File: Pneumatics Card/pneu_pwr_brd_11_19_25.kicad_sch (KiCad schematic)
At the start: 62 parts, among them J1 2X1, J10 Conn_01x02, J11 Conn_01x02, J12 2X1, J2 2X1, J3 2X1, J4 2X1, J5 2X1, J6 2X1, J7 Conn_01x03_Pin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

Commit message: Testing_Anthony
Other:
- note added: "NEED BJTS KEEP CAPs THE SAME for NOW HOLES VIAS VIAS VIAS"
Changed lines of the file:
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@@
 	(generator_version "9.0")
 	(paper "A2")
+	(text "NEED BJTS\nKEEP CAPs THE SAME for NOW\nHOLES\nVIAS VIAS VIAS"
+		(exclude_from_sim no)
+		(at 169.926 298.704 0)
+		(effects
+			(font
+				(size 1.27 1.27)
+			)
+		)
+	)
 	(text "HSE\n"
 		(exclude_from_sim no)

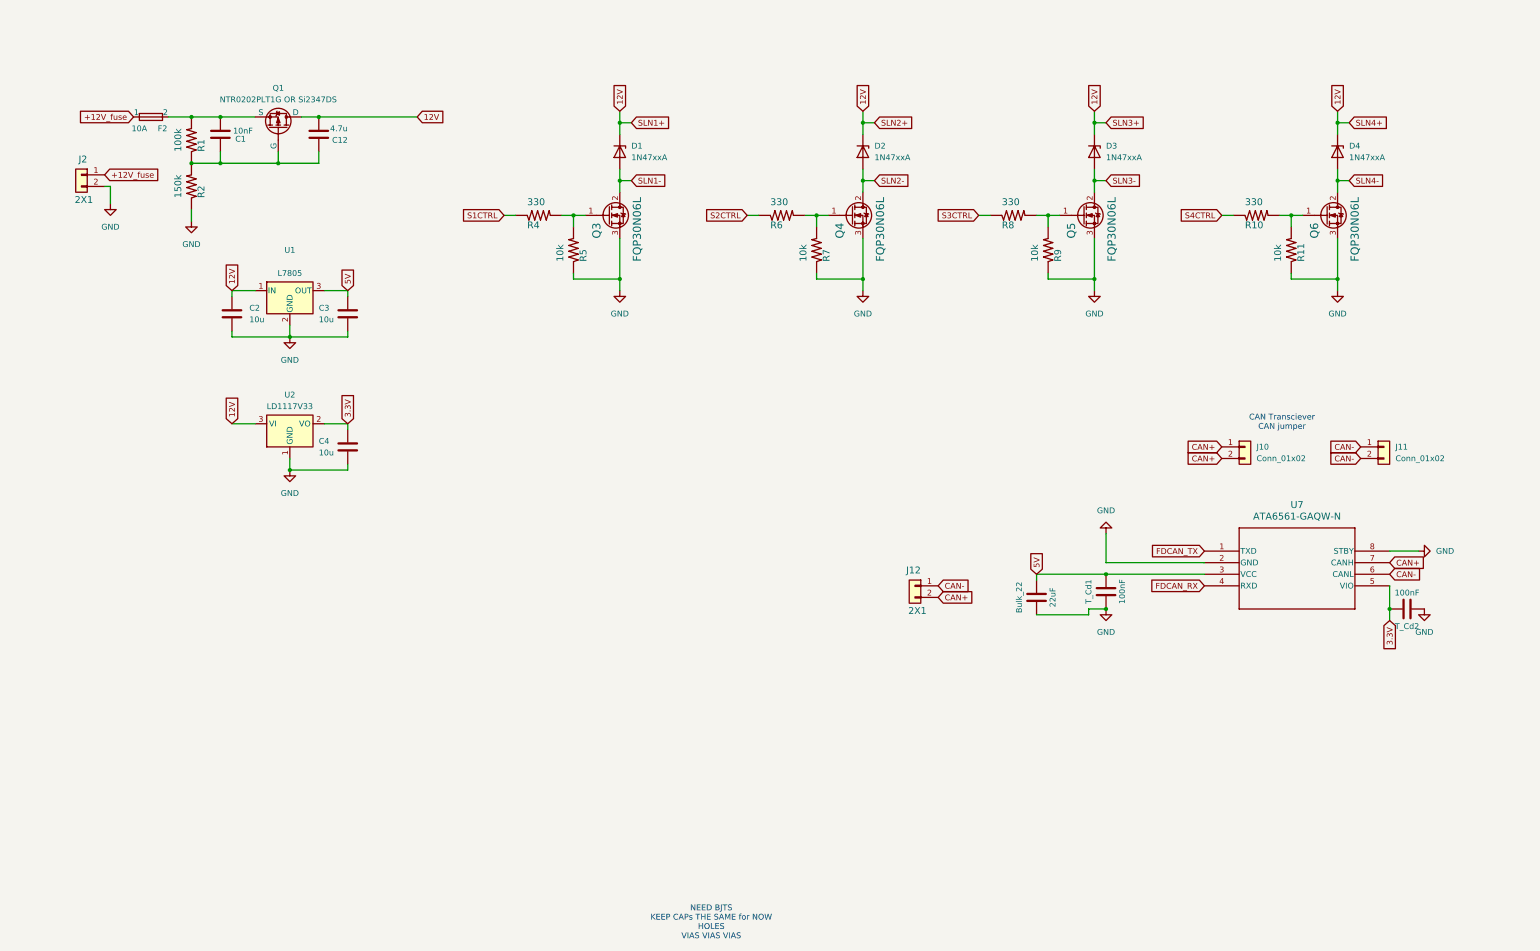
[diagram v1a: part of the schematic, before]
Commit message: Added the Mosfet drivers
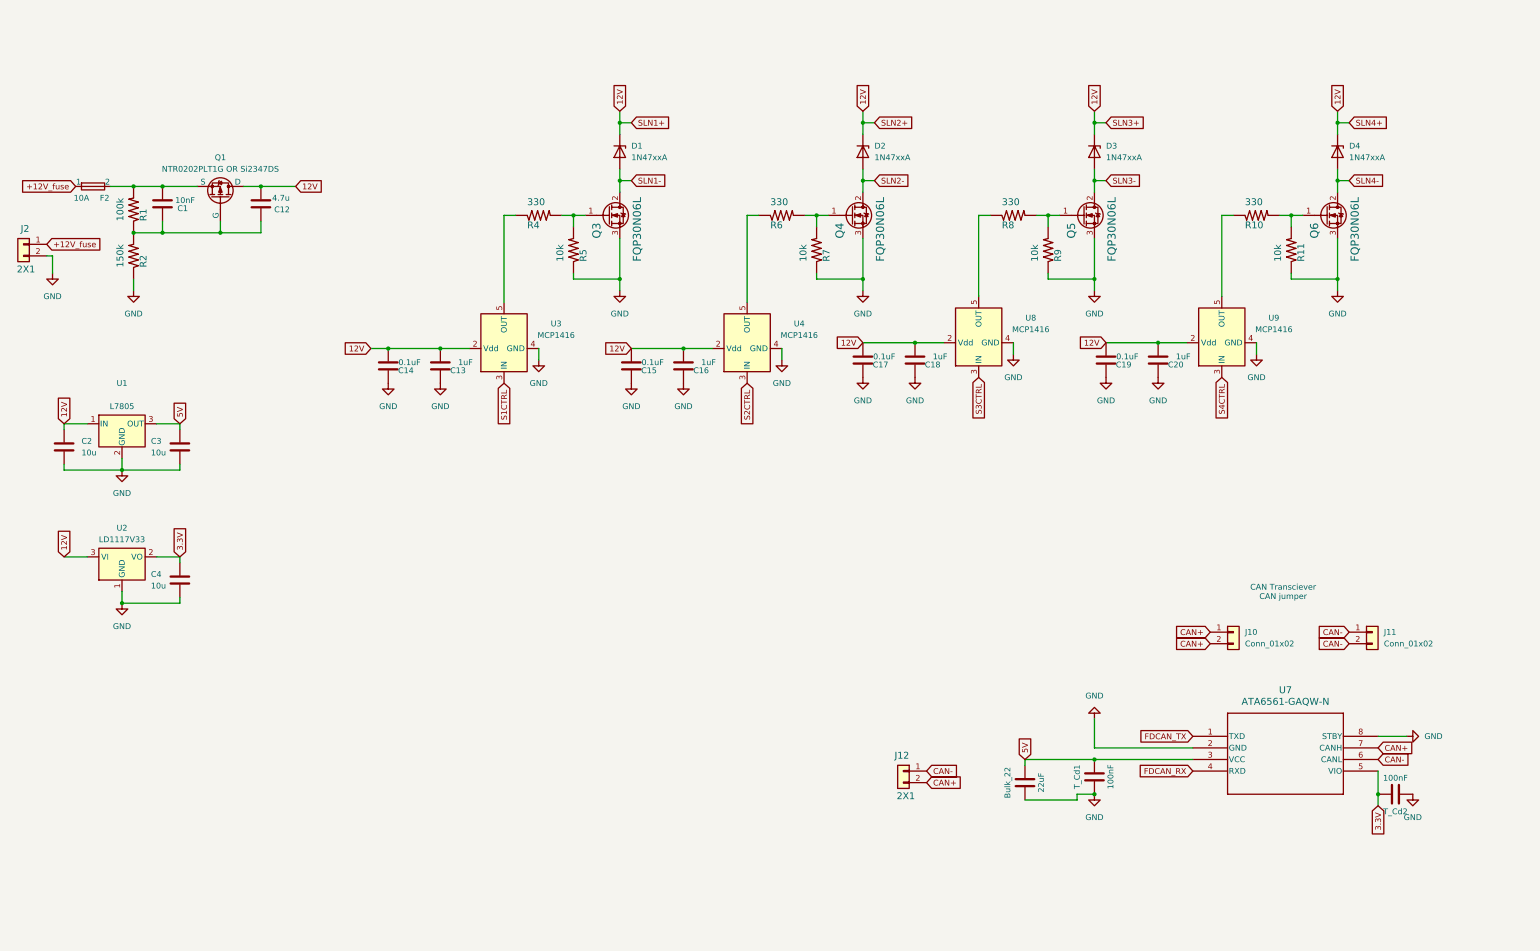
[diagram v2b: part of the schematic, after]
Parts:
- added C13, C16, C18, C20: 1uF, Capacitor_SMD:C_0402_1005Metric, symbol Device:C
- added C14, C15, C17, C19: 0.1uF, Capacitor_SMD:C_0402_1005Metric, symbol Device:C
- added U3, U4, U8, U9: MCP1416, Package_TO_SOT_SMD:SOT-23-5, symbol Driver_FET:MCP1416
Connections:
- net 12V: now also C13.2, C14.2, C15.2, C16.2, C17.2, C18.2, C19.2, C20.2, U3.2 (Vdd), U4.2 (Vdd), U8.2 (Vdd), U9.2 (Vdd)
- net GND: now also C13.1, C14.1, C15.1, C16.1, C17.1, C18.1, C19.1, C20.1, U3.4 (GND), U4.4 (GND), U8.4 (GND), U9.4 (GND)
- net S1CTRL: now also U3.3 (IN); no longer R4.1
- net S2CTRL: now also U4.3 (IN); no longer R6.1
- net S3CTRL: now also U8.3 (IN); no longer R8.1
- net S4CTRL: now also U9.3 (IN); no longer R10.1
- new net: R4.1, U3.5 (OUT)
- new net: R10.1, U9.5 (OUT)
- new net: R8.1, U8.5 (OUT)
- new net: R6.1, U4.5 (OUT)
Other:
- note removed: "NEED BJTS KEEP CAPs THE SAME for NOW HOLES VIAS VIAS VIAS"
- moved on the sheet: Bulk_22, C1, C12, C2, C3, C4, F2, J10, J11, J12, J2, Q1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

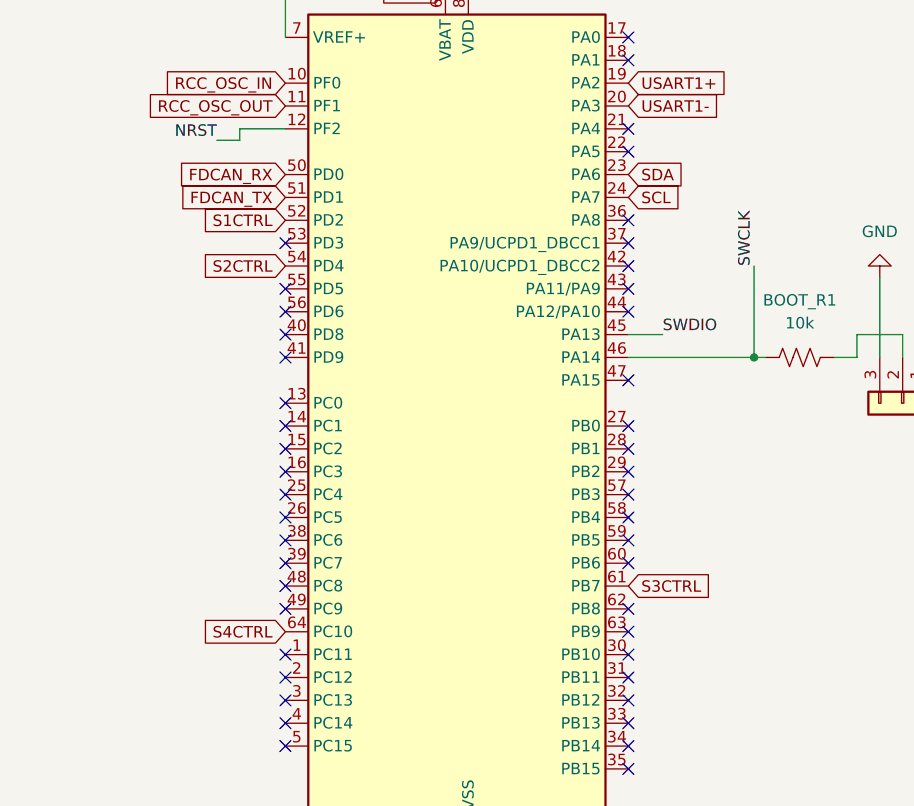
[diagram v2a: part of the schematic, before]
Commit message: Redid the Layout with new components
Increased board size to 63x63mm, added mounting holes (need to recheck), traces not routed yet.
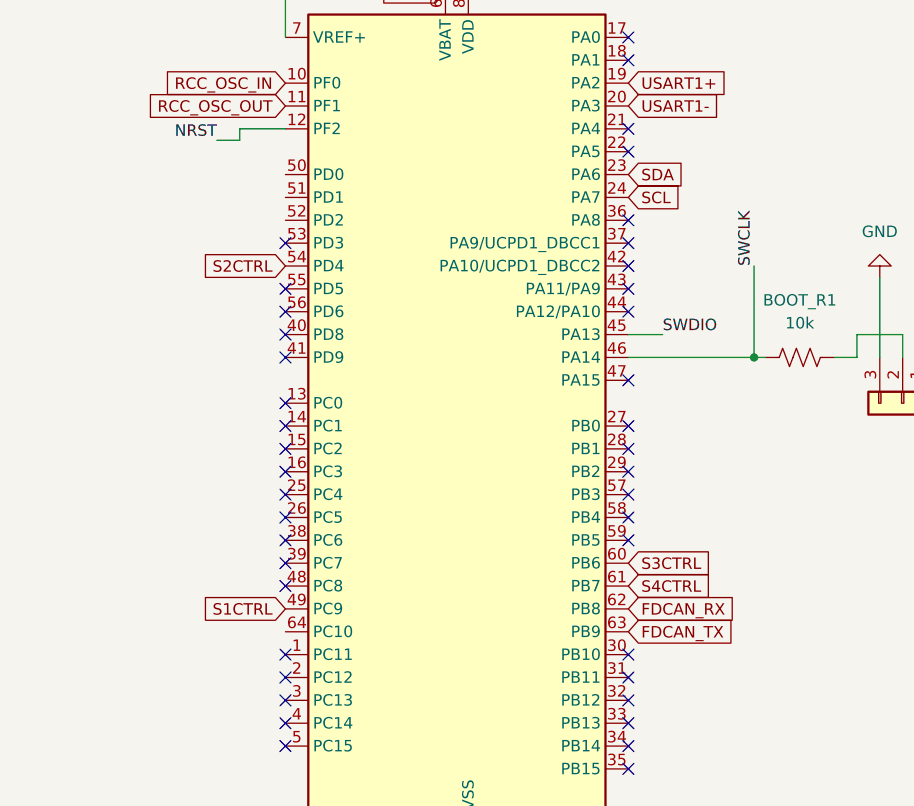
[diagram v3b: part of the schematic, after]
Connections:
- net FDCAN_RX: now also U6.62 (PB8); no longer U6.50 (PD0)
- net FDCAN_TX: now also U6.63 (PB9); no longer U6.51 (PD1)
- net S1CTRL: now also U6.49 (PC9); no longer U6.52 (PD2)
- net S3CTRL: now also U6.60 (PB6); no longer U6.61 (PB7)
- net S4CTRL: now also U6.61 (PB7); no longer U6.64 (PC10)
- no-connect marks 45 -> 41
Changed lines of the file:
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@@
 	)
 	(no_connect
-		(at 410.21 143.51)
-	)
-	(no_connect
 		(at 410.21 107.95)
 	)
@@
 	)
 	(no_connect
-		(at 372.11 143.51)
-	)
-	(no_connect
 		(at 372.11 151.13)
 	)
@@
 	)
 	(no_connect
-		(at 410.21 138.43)
-	)
-	(no_connect
 		(at 372.11 102.87)
 	)
 	(no_connect
-		(at 410.21 146.05)
-	)
-	(no_connect
 		(at 372.11 135.89)
 	)
@@
 	(global_label "FDCAN_RX"
 		(shape input)
-		(at 372.11 95.25 180)
+		(at 410.21 143.51 0)
 		(fields_autoplaced yes)
 		(effects
@@
 				(size 1.27 1.27)
 			)
-			(justify right)
+			(justify left)
 		)
 		(property "Intersheetrefs" "${INTERSHEET_REFS}"
-			(at 359.63 95.25 0)
+			(at 422.69 143.51 0)
 			(effects
 				(font
 					(size 1.27 1.27)
 				)
-				(justify right)
+				(justify left)
 				(hide yes)
 			)
@@
 	(global_label "S4CTRL"
 		(shape input)
-		(at 372.11 146.05 180)
+		(at 410.21 140.97 0)
 		(fields_autoplaced yes)
 		(effects
@@
 				(size 1.27 1.27)
 			)
-			(justify right)
+			(justify left)
 		)
 		(property "Intersheetrefs" "${INTERSHEET_REFS}"
-			(at 362.1701 146.05 0)
+			(at 420.1499 140.97 0)
 			(effects
 				(font
 					(size 1.27 1.27)
 				)
-				(justify right)
+				(justify left)
 				(hide yes)
 			)
@@
 	(global_label "FDCAN_TX"
 		(shape input)
-		(at 372.11 97.79 180)
+		(at 410.21 146.05 0)
 		(fields_autoplaced yes)
 		(effects
@@
 				(size 1.27 1.27)
 			)
-			(justify right)
+			(justify left)
 		)
 		(property "Intersheetrefs" "${INTERSHEET_REFS}"
-			(at 359.9324 97.79 0)
+			(at 422.3876 146.05 0)
 			(effects
 				(font
 					(size 1.27 1.27)
 				)
-				(justify right)
+				(justify left)
 				(hide yes)
 			)
@@
 	(global_label "S1CTRL"
 		(shape input)
-		(at 372.11 100.33 180)
+		(at 372.11 143.51 180)
 		(fields_autoplaced yes)
 		(effects
@@
 		)
 		(property "Intersheetrefs" "${INTERSHEET_REFS}"
-			(at 362.1701 100.33 0)
+			(at 362.1701 143.51 0)
 			(effects
 				(font
@@
 	(global_label "S3CTRL"
 		(shape input)
-		(at 410.21 140.97 0)
+		(at 410.21 138.43 0)
 		(fields_autoplaced yes)
 		(effects
@@
 		)
 		(property "Intersheetrefs" "${INTERSHEET_REFS}"
-			(at 420.1499 140.97 0)
+			(at 420.1499 138.43 0)
 			(effects
 				(font

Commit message: Fixed the footprints and silkscreens
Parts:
- U5: footprint TCA4307:SOP65P490X110-8N -> custom_components:SOIC8_DGK_TEX
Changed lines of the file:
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@@
 			)
 		)
-		(property "Footprint" "TCA4307:SOP65P490X110-8N"
+		(property "Footprint" "custom_components:SOIC8_DGK_TEX"
 			(at 99.06 64.77 0)
 			(effects

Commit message: Made most of routing
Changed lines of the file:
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@@
 	)
 	(junction
+		(at 77.47 137.16)
+		(diameter 0)
+		(color 0 0 0 0)
+	)
+	(junction
 		(at 99.06 172.72)
 		(diameter 0)
@@
 	(wire
 		(pts
-			(xy 71.12 137.16) (xy 78.74 137.16)
+			(xy 71.12 137.16) (xy 77.47 137.16)
 		)
 		(stroke
@@
 	(wire
 		(pts
+			(xy 77.47 130.81) (xy 77.47 137.16)
+		)
+		(stroke
+			(width 0)
+			(type default)
+		)
+	)
+	(wire
+		(pts
 			(xy 410.21 115.57) (xy 424.18 115.57)
 		)
@@
 	(wire
 		(pts
+			(xy 77.47 137.16) (xy 78.74 137.16)
+		)
+		(stroke
+			(width 0)
+			(type default)
+		)
+	)
+	(wire
+		(pts
 			(xy 67.31 81.28) (xy 67.31 86.36)
 		)
@@
 					(unit 1)
 				)
+			)
+		)
+	)
+	(symbol
+		(lib_id "power:PWR_FLAG")
+		(at 77.47 130.81 0)
+		(unit 1)
+		(exclude_from_sim no)
+		(in_bom yes)
+		(on_board yes)
+		(dnp no)
+		(fields_autoplaced yes)
+		(property "Reference" "#FLG02"
+			(at 77.47 128.905 0)
+			(effects
+				(font
+					(size 1.27 1.27)
+				)
+				(hide yes)
+			)
+		)
+		(property "Value" "PWR_FLAG"
+			(at 77.47 125.73 0)
+			(effects
+				(font
+					(size 1.27 1.27)
+				)
+			)
+		)
+		(property "Footprint" ""
+			(at 77.47 130.81 0)
+			(effects
+				(font
+					(size 1.27 1.27)
+				)
+				(hide yes)
+			)
+		)
+		(property "Datasheet" "~"
+			(at 77.47 130.81 0)
+			(effects
+				(font
+					(size 1.27 1.27)
+				)
+				(hide yes)
+			)
+		)
+		(property "Description" "Special symbol for telling ERC where power comes from"
+			(at 77.47 130.81 0)
+			(effects
+				(font
+					(size 1.27 1.27)
+				)
+				(hide yes)
+			)
+		)
+		(pin "1"
+		)
+		(instances
+			(project ""
+				(path "/c299c6f2-212e-472c-8577-e7ed124513dd"
+					(reference "#FLG02")
+					(unit 1)
+				)
